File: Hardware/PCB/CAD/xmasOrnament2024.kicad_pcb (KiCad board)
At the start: 2 copper layers, 60 x 66.9 mm, 56 parts, among them IC1 TP4056-42, Q1 AO3401A, Q2 CJ3400, SW1 BZCN_TSA007A1518B03, SW2 BZCN_TSA007A1518B03, U1 STM32C011F6, U2 TPS7A2633DRVR

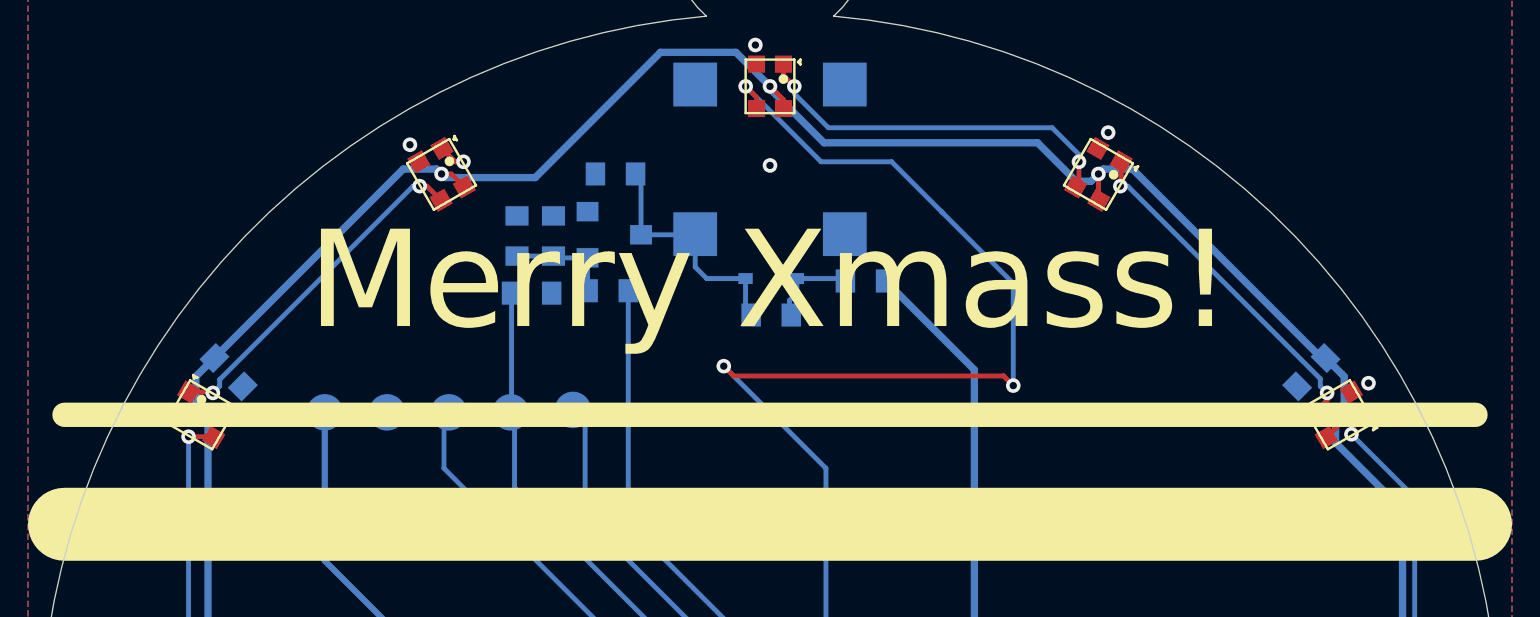
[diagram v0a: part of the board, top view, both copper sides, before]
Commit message: Sync - Changed typo on PCB.
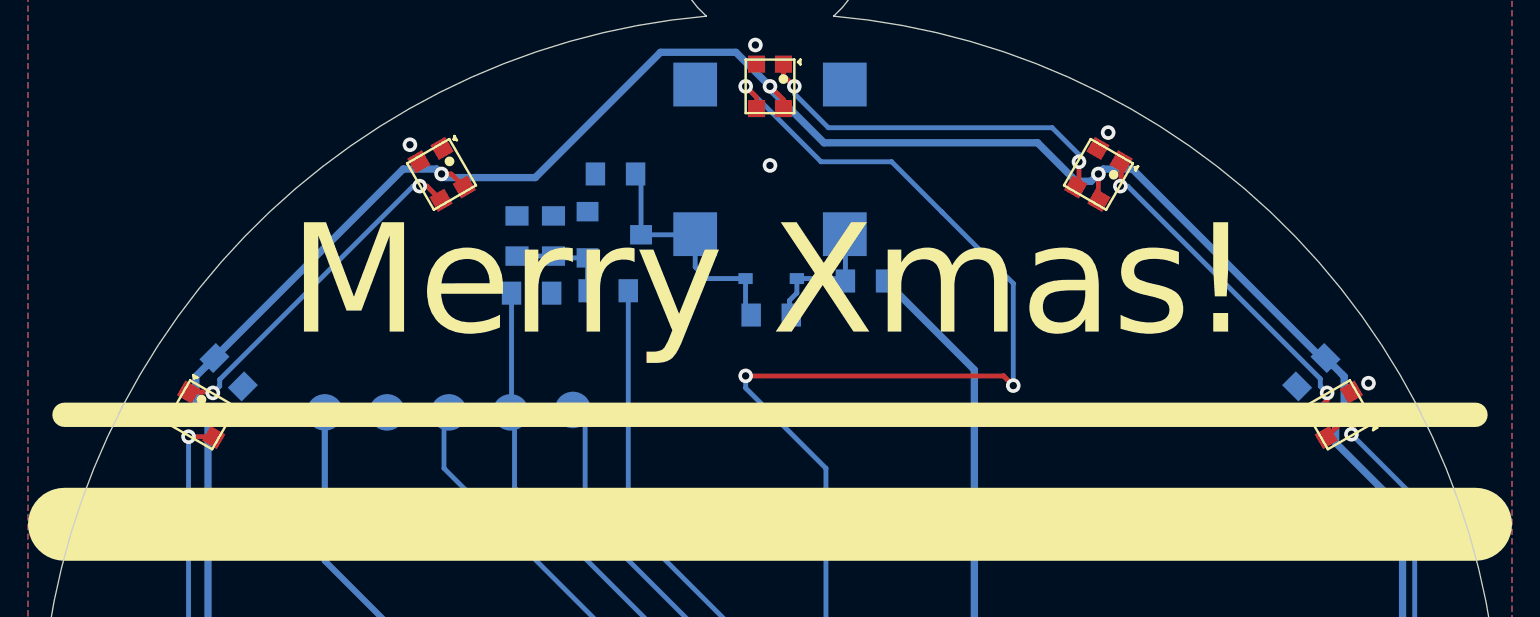
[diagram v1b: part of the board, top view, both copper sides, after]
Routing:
- net /WS_DIN: track 50.4 -> 48.5 mm
- net unconnected-(LED13-DO-Pad1): track 1.11 -> 0.00 mm, vias 1 -> 0
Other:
- board text added: "Borna Biro 2024."
- board text added: "Merry Xmas!"
- board text removed: "Merry Xmass!"
